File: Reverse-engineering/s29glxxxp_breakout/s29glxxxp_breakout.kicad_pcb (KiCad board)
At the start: 2 copper layers, 45 x 28 mm, 5 parts, among them J1 ADDR, J2 DAT, U1 EN29GL256

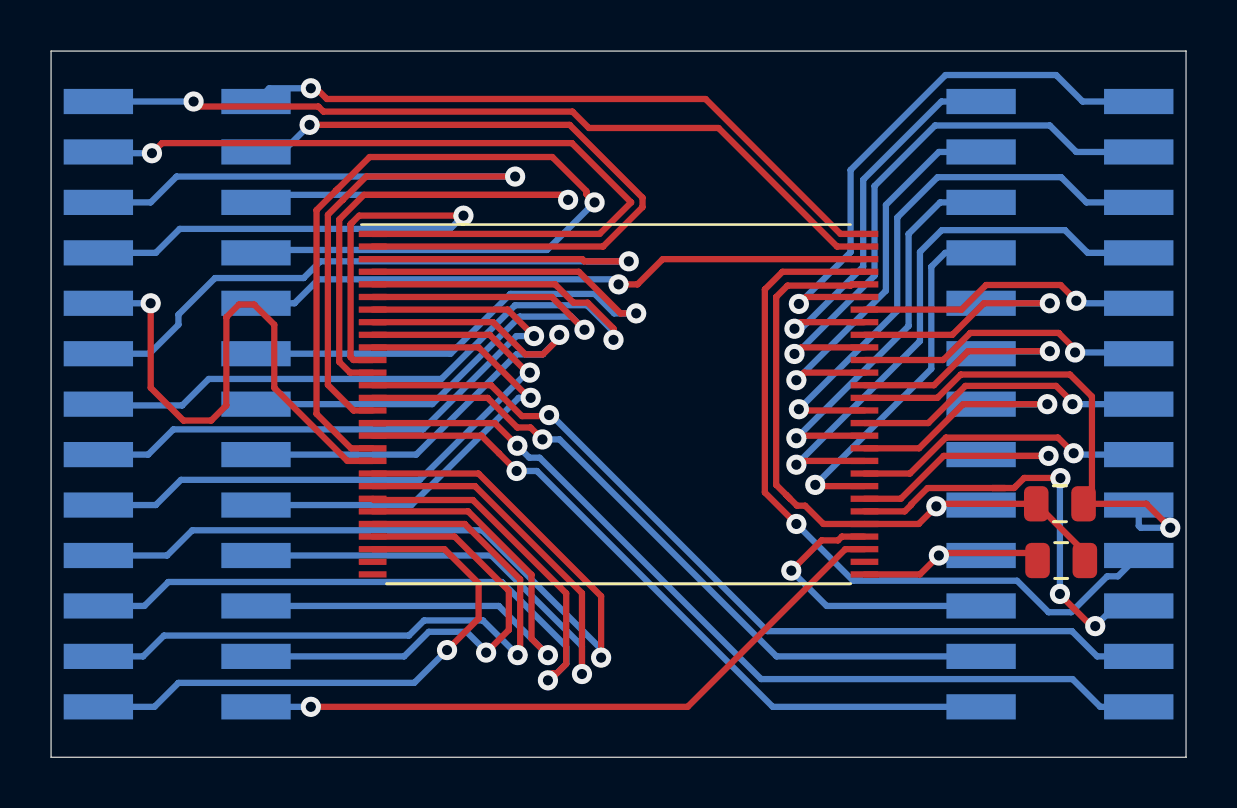
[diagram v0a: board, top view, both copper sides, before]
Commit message: Changing the outline of the S29GLxxxP breakout so that it's a tad more panel-friendly
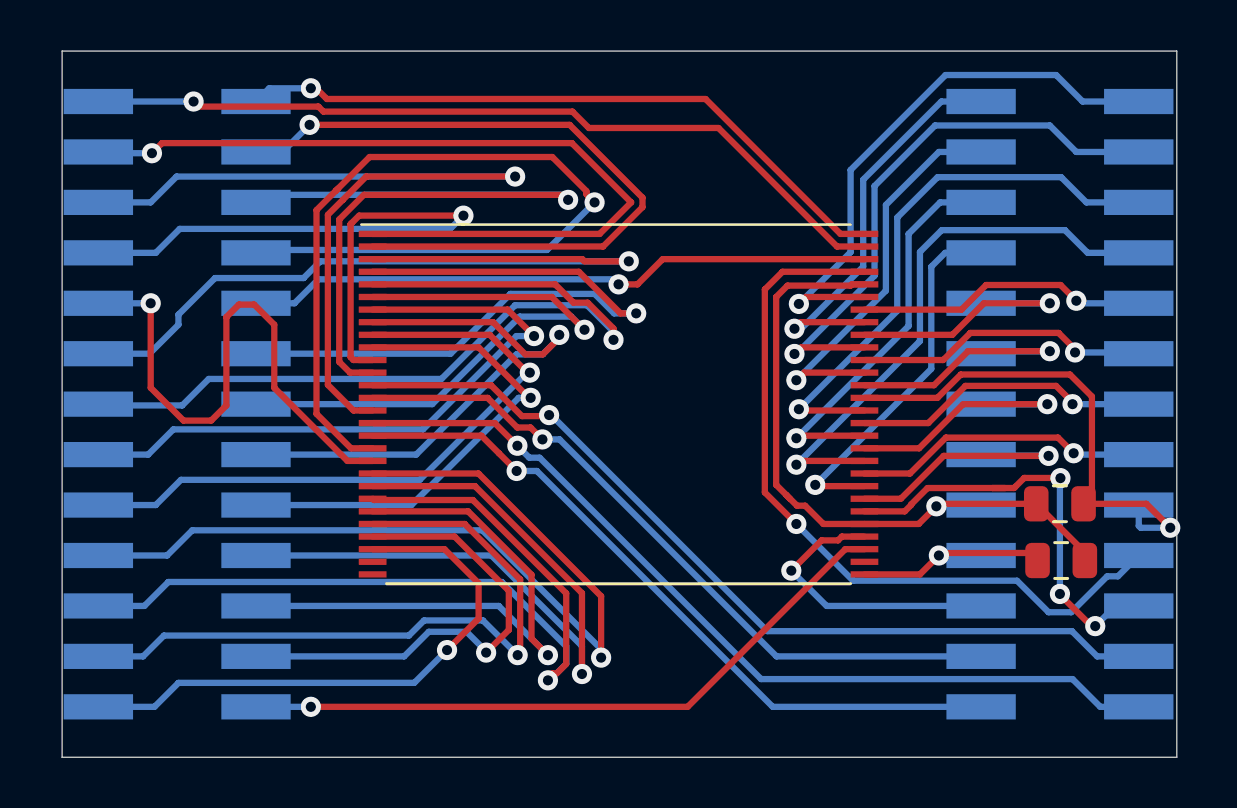
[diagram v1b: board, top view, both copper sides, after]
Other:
- board size 45 x 28 mm -> 44.2 x 28 mm
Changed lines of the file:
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@@
     (pad_to_mask_clearance 0.051)
     (solder_mask_min_width 0.25)
-    (aux_axis_origin 120 107.65)
+    (aux_axis_origin 119.634 107.65)
     (visible_elements 7FFFFFFF)
     (pcbplotparams
@@
     )
   )
-  (gr_line (start 120 135.65) (end 120 107.65) (layer Edge.Cuts) (width 0.05))
-  (gr_line (start 75 135.65) (end 120 135.65) (layer Edge.Cuts) (width 0.05))
-  (gr_line (start 75 107.65) (end 75 135.65) (layer Edge.Cuts) (width 0.05))
-  (gr_line (start 120 107.65) (end 75 107.65) (layer Edge.Cuts) (width 0.05))
+  (gr_line (start 119.634 135.65) (end 119.634 107.65) (layer Edge.Cuts) (width 0.05))
+  (gr_line (start 75.438 135.65) (end 119.634 135.65) (layer Edge.Cuts) (width 0.05))
+  (gr_line (start 75.438 107.65) (end 75.438 135.65) (layer Edge.Cuts) (width 0.05))
+  (gr_line (start 119.634 107.65) (end 75.438 107.65) (layer Edge.Cuts) (width 0.05))
   (via (at 110.1 125.7) (size 0.8) (drill 0.4) (layers F.Cu B.Cu) (net 1))
   (segment (start 114.0625 125.6) (end 110.2 125.6) (width 0.25) (layer F.Cu) (net 1))
